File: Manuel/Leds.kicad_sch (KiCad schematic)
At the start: 33 parts, among them U5 ULN2003

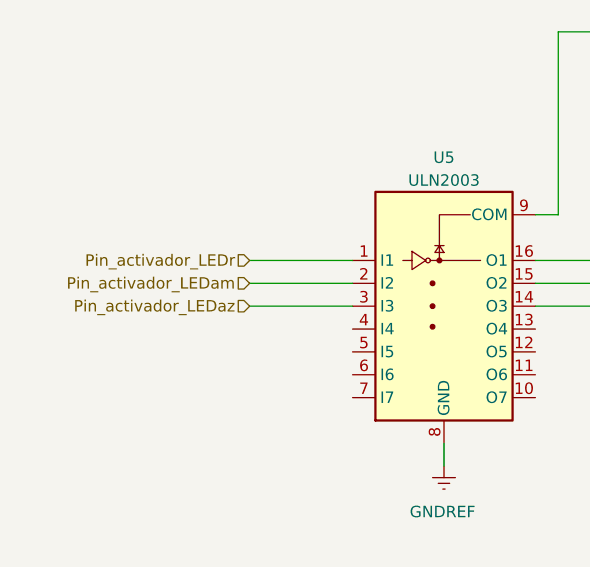
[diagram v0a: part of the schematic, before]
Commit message: Proyecto Kiss V2
Esquemático y PCB terminados
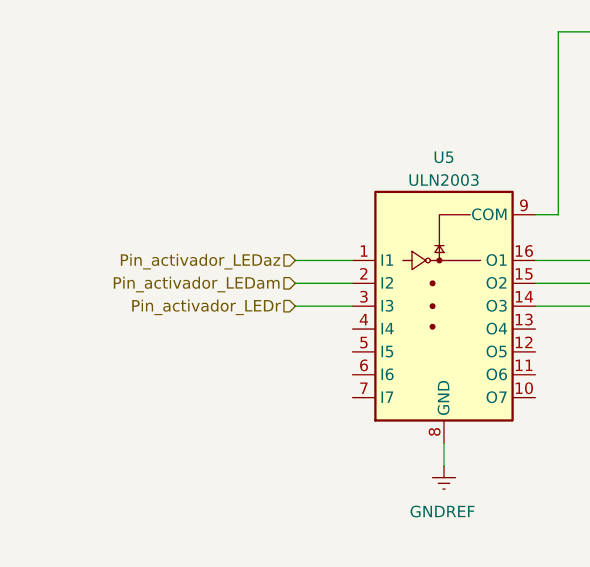
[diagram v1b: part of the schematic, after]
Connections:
- net Pin_activador_LEDaz: now also U5.1 (I1); no longer U5.3 (I3)
- net Pin_activador_LEDr: now also U5.3 (I3); no longer U5.1 (I1)
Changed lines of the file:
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@@
-    (stroke (width 0) (type default))
-  )
-  (wire (pts (xy 71.755 99.695) (xy 83.185 99.695))
     (stroke (width 0) (type default))
   )
@@
     (stroke (width 0) (type default))
   )
-  (wire (pts (xy 71.755 102.235) (xy 83.185 102.235))
-    (stroke (width 0) (type default))
-  )
   (wire (pts (xy 186.69 85.725) (xy 186.69 89.535))
     (stroke (width 0) (type default))
@@
     (stroke (width 0) (type default))
   )
+  (wire (pts (xy 76.835 102.235) (xy 83.185 102.235))
+    (stroke (width 0) (type default))
+  )
   (wire (pts (xy 149.225 99.695) (xy 140.335 99.695))
     (stroke (width 0) (type default))
@@
     (stroke (width 0) (type default))
   )
+  (wire (pts (xy 76.835 104.775) (xy 83.185 104.775))
+    (stroke (width 0) (type default))
+  )
   (wire (pts (xy 213.36 99.695) (xy 204.47 99.695))
     (stroke (width 0) (type default))
@@
     (stroke (width 0) (type default))
   )
-  (wire (pts (xy 71.755 104.775) (xy 83.185 104.775))
-    (stroke (width 0) (type default))
-  )
   (wire (pts (xy 168.91 74.295) (xy 158.115 74.295))
+    (stroke (width 0) (type default))
+  )
+  (wire (pts (xy 76.835 99.695) (xy 83.185 99.695))
     (stroke (width 0) (type default))
   )
@@
     )
   )
-  (hierarchical_label "Pin_activador_LEDam" (shape input) (at 71.755 102.235 180) (fields_autoplaced)
+  (hierarchical_label "Pin_activador_LEDam" (shape input) (at 76.835 102.235 180) (fields_autoplaced)
     (effects (font (size 1.27 1.27)) (justify right))
   )
-  (hierarchical_label "Pin_activador_LEDr" (shape input) (at 71.755 99.695 180) (fields_autoplaced)
+  (hierarchical_label "Pin_activador_LEDr" (shape input) (at 76.835 104.775 180) (fields_autoplaced)
     (effects (font (size 1.27 1.27)) (justify right))
   )
-  (hierarchical_label "Pin_activador_LEDaz" (shape input) (at 71.755 104.775 180) (fields_autoplaced)
+  (hierarchical_label "Pin_activador_LEDaz" (shape input) (at 76.835 99.695 180) (fields_autoplaced)
     (effects (font (size 1.27 1.27)) (justify right))
   )
